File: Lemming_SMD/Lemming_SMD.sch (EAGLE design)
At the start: 35 parts, among them Q1 2SA1203, Q11 SS8050, Q12 2SA1203, Q2 SS8050, Q3 2SA1203, Q4 SS8050, Q5 2SA1203, Q6 SS8050, U3 BME280, X1 I2C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

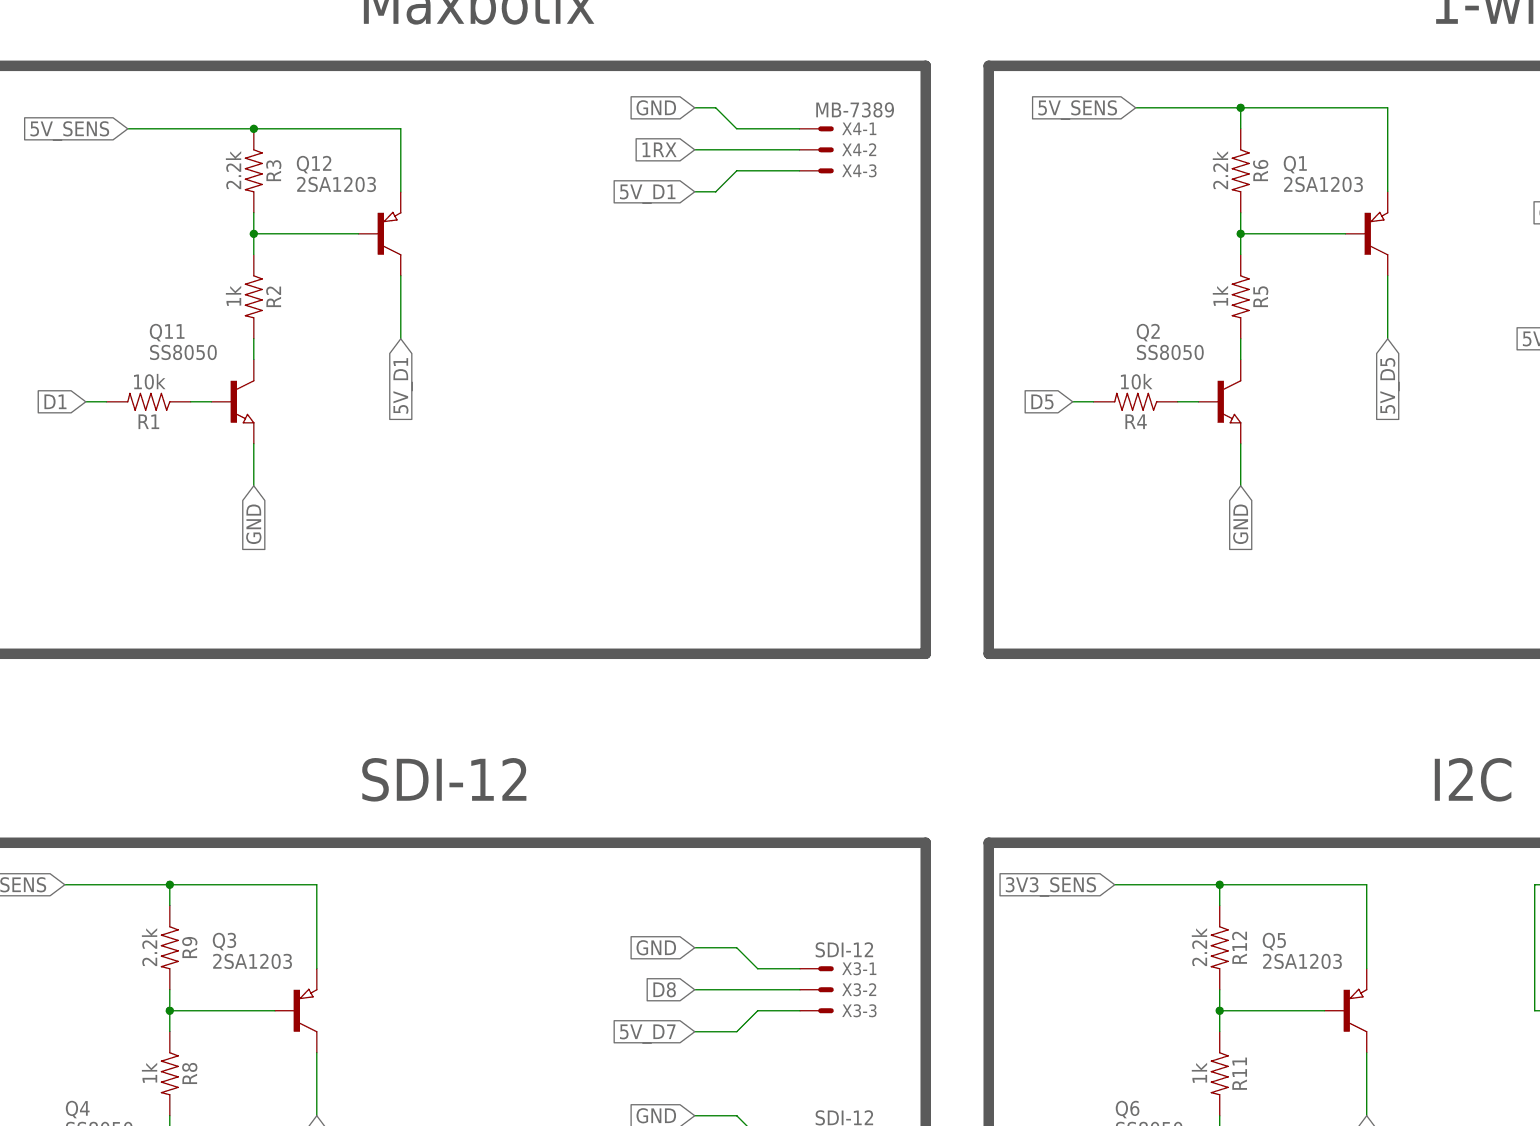
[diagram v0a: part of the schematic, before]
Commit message: Ordered Version 1.0 from Seeed
Lemming_SMD V1.0
Lagopus_A V1.0
Lagopus_B V1.0
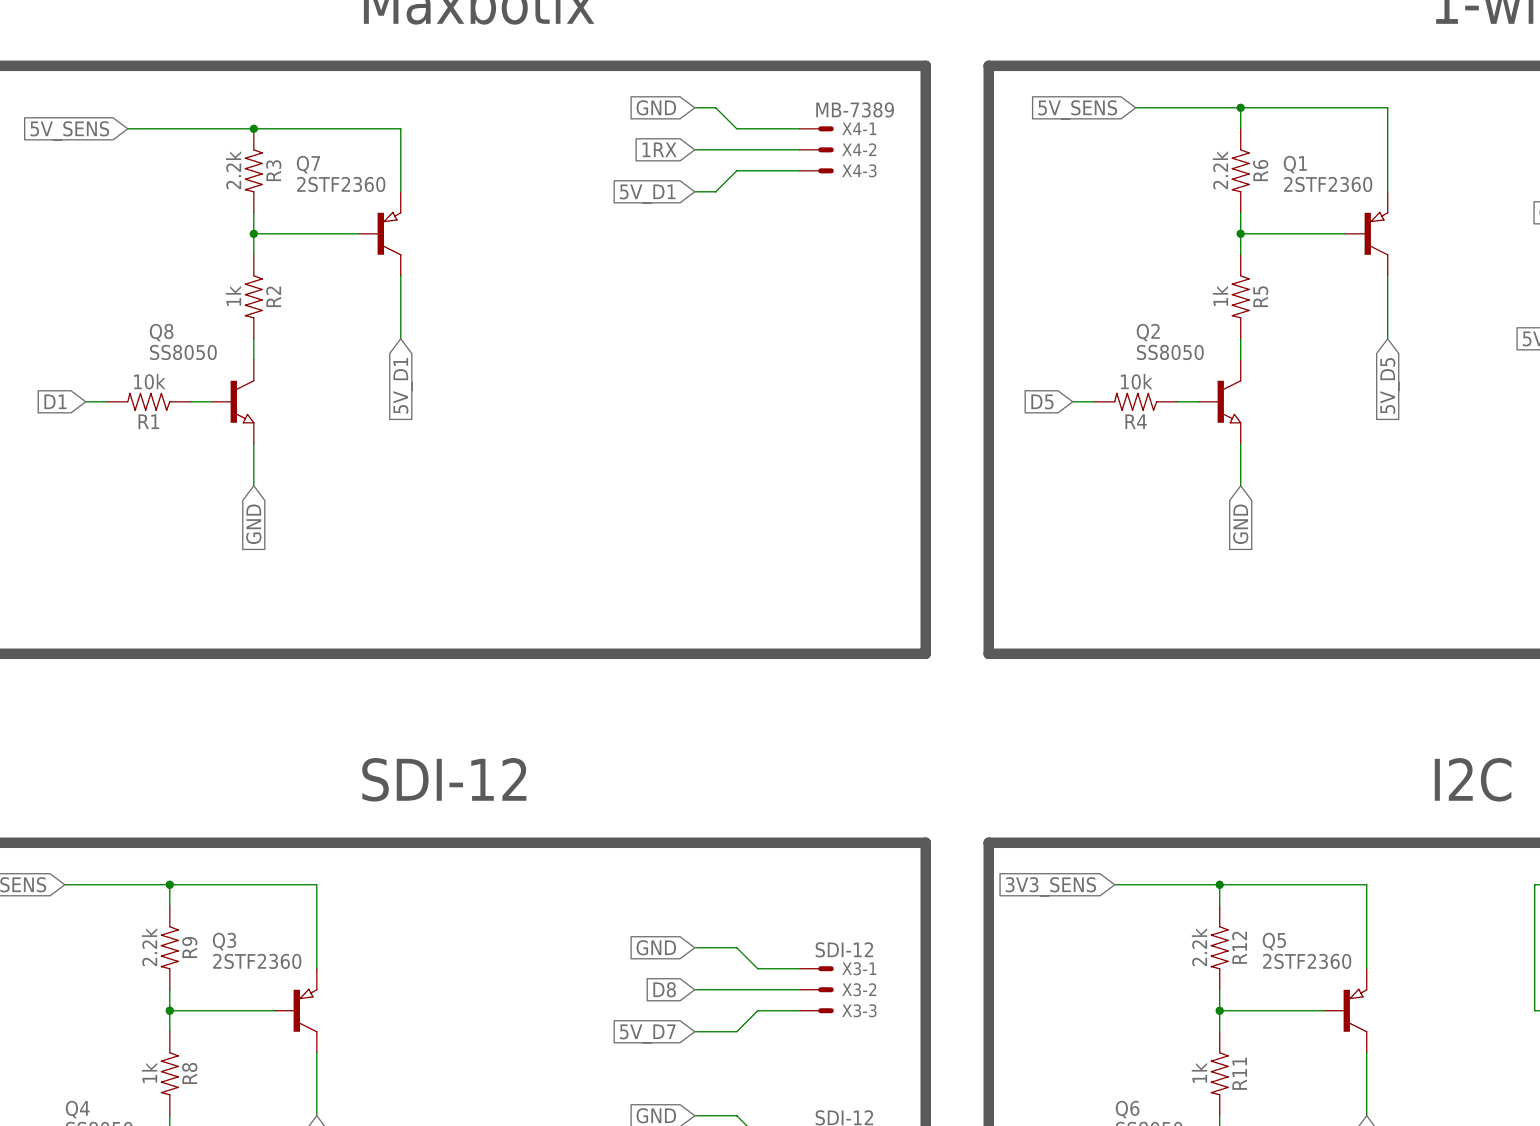
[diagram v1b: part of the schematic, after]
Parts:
- Q1, Q3, Q5, Q7: value 2SA1203 -> 2STF2360
- renumbered Q11 to Q8, Q12 to Q7

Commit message: Lemming SMD new order 2020
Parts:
- JP1: value JUMPER-SMT_3_2-NC_PASTE_SILK -> JUMPER-SMT_3_NO_SILK; device SparkFun-Jumpers:JUMPER-SMT_3_2-NC_PASTE_SILK -> SparkFun-Jumpers:JUMPER-SMT_3_NO_SILK
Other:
- note removed: "Clear JP1 to remove I2C pullups from bus"

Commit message: Minor changes befor order
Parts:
- added X8: IRIDIUM, con-molex:22-23-2031
- added X9: IRIDIUM-2, con-molex:22-23-2031
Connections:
- net 2RX: now also X8-1.S
- net 2TX: now also X8-2.S
- net BATTERY: now also X9-1.S
- net D4: now also X8-3.S
- net GND: now also X9-2.S, X9-3.S
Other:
- note added: "IRIDIUM"
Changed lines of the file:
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@@
 <part name="X7" library="con-molex" deviceset="22-23-2031" device="" value="SDI-12"/>
 <part name="JP1" library="SparkFun-Jumpers" library_urn="urn:adsk.eagle:library:528" deviceset="JUMPER-SMT_3_NO" device="_SILK" package3d_urn="urn:adsk.eagle:package:39285/1"/>
+<part name="X8" library="con-molex" deviceset="22-23-2031" device="" value="IRIDIUM"/>
+<part name="X9" library="con-molex" deviceset="22-23-2031" device="" value="IRIDIUM-2"/>
 </parts>
 <sheets>
@@
 <text x="-273.304" y="-106.172" size="1.778" layer="97" align="top-left">BME280 is configured to I2C mode</text>
 <text x="-256.54" y="-53.34" size="5.08" layer="97">BME280</text>
+<text x="-17.78" y="129.54" size="5.08" layer="97">IRIDIUM</text>
+<wire x1="20.32" y1="124.46" x2="-33.02" y2="124.46" width="1.27" layer="97"/>
+<wire x1="-33.02" y1="124.46" x2="-33.02" y2="53.34" width="1.27" layer="97"/>
+<wire x1="20.32" y1="53.34" x2="20.32" y2="124.46" width="1.27" layer="97"/>
+<wire x1="-33.02" y1="53.34" x2="20.32" y2="53.34" width="1.27" layer="97"/>
 </plain>
 <instances>
@@
 <attribute name="NAME" x="-99.06" y="10.541" size="1.778" layer="95" font="vector"/>
 </instance>
+<instance part="X8" gate="-1" x="5.08" y="101.6" smashed="yes">
+<attribute name="NAME" x="7.62" y="100.838" size="1.524" layer="95"/>
+<attribute name="VALUE" x="4.318" y="102.997" size="1.778" layer="96"/>
+</instance>
+<instance part="X8" gate="-2" x="5.08" y="99.06" smashed="yes">
+<attribute name="NAME" x="7.62" y="98.298" size="1.524" layer="95"/>
+</instance>
+<instance part="X8" gate="-3" x="5.08" y="96.52" smashed="yes">
+<attribute name="NAME" x="7.62" y="95.758" size="1.524" layer="95"/>
+</instance>
+<instance part="X9" gate="-1" x="5.08" y="86.36" smashed="yes">
+<attribute name="NAME" x="7.62" y="85.598" size="1.524" layer="95"/>
+<attribute name="VALUE" x="4.318" y="87.757" size="1.778" layer="96"/>
+</instance>
+<instance part="X9" gate="-2" x="5.08" y="83.82" smashed="yes">
+<attribute name="NAME" x="7.62" y="83.058" size="1.524" layer="95"/>
+</instance>
+<instance part="X9" gate="-3" x="5.08" y="81.28" smashed="yes">
+<attribute name="NAME" x="7.62" y="80.518" size="1.524" layer="95"/>
+</instance>
 </instances>
 <busses>
@@
 <wire x1="-162.56" y1="-104.14" x2="-167.64" y2="-104.14" width="0.1524" layer="91"/>
 <label x="-167.64" y="-104.14" size="1.27" layer="95" rot="R180" xref="yes"/>
+</segment>
+<segment>
+<wire x1="-2.54" y1="93.98" x2="-5.08" y2="93.98" width="0.1524" layer="91"/>
+<label x="-5.08" y="93.98" size="1.778" layer="95" rot="R180" xref="yes"/>
+<pinref part="X8" gate="-3" pin="S"/>
+<wire x1="2.54" y1="96.52" x2="0" y2="96.52" width="0.1524" layer="91"/>
+<wire x1="0" y1="96.52" x2="-2.54" y2="93.98" width="0.1524" layer="91"/>
 </segment>
 </net>
@@
 <wire x1="-203.2" y1="-22.86" x2="-198.12" y2="-22.86" width="0.1524" layer="91"/>
 </segment>
+<segment>
+<wire x1="2.54" y1="83.82" x2="-5.08" y2="83.82" width="0.1524" layer="91"/>
+<label x="-5.08" y="83.82" size="1.778" layer="95" rot="R180" xref="yes"/>
+<pinref part="X9" gate="-2" pin="S"/>
+</segment>
+<segment>
+<wire x1="-2.54" y1="78.74" x2="-5.08" y2="78.74" width="0.1524" layer="91"/>
+<label x="-5.08" y="78.74" size="1.778" layer="95" rot="R180" xref="yes"/>
+<pinref part="X9" gate="-3" pin="S"/>
+<wire x1="2.54" y1="81.28" x2="0" y2="81.28" width="0.1524" layer="91"/>
+<wire x1="0" y1="81.28" x2="-2.54" y2="78.74" width="0.1524" layer="91"/>
+</segment>
 </net>
 <net name="1RX" class="0">
@@
 <label x="-137.16" y="-137.16" size="1.27" layer="95" rot="R270" xref="yes"/>
 </segment>
+<segment>
+<wire x1="2.54" y1="99.06" x2="-5.08" y2="99.06" width="0.1524" layer="91"/>
+<label x="-5.08" y="99.06" size="1.778" layer="95" rot="R180" xref="yes"/>
+<pinref part="X8" gate="-2" pin="S"/>
+</segment>
 </net>
 <net name="2RX" class="0">
@@
 <wire x1="-132.08" y1="-127" x2="-132.08" y2="-137.16" width="0.1524" layer="91"/>
 <label x="-132.08" y="-137.16" size="1.27" layer="95" rot="R270" xref="yes"/>
+</segment>
+<segment>
+<label x="-5.08" y="104.14" size="1.778" layer="95" rot="R180" xref="yes"/>
+<wire x1="-2.54" y1="104.14" x2="-5.08" y2="104.14" width="0.1524" layer="91"/>
+<pinref part="X8" gate="-1" pin="S"/>
+<wire x1="2.54" y1="101.6" x2="0" y2="101.6" width="0.1524" layer="91"/>
+<wire x1="0" y1="101.6" x2="-2.54" y2="104.14" width="0.1524" layer="91"/>
 </segment>
 </net>
@@
 <label x="-106.68" y="-137.16" size="1.27" layer="95" rot="R270" xref="yes"/>
 </segment>
-</net>
+<segment>
+<label x="-5.08" y="88.9" size="1.778" layer="95" rot="R180" xref="yes"/>
+<wire x1="-2.54" y1="88.9" x2="-5.08" y2="88.9" width="0.1524" layer="91"/>
+<pinref part="X9" gate="-1" pin="S"/>
+<wire x1="2.54" y1="86.36" x2="0" y2="86.36" width="0.1524" layer="91"/>
+<wire x1="0" y1="86.36" x2="-2.54" y2="88.9" width="0.1524" layer="91"/>
+</segment>
+</net>
